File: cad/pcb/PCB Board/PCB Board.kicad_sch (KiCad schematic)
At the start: 40 parts, among them J1 USB4105, J2 S2B-PH-K-S, Q1 FDN340P, Q2 BSS138, SW1 PTS645, SW2 PTS645, SW3 PTS645, SW4 PTS645, SW5 PTS645, SW6 PTS645, SW7 SLW-1277545-3A-RA-N-D, U1 ESP32-C3-WROOM-02, U2 TLV75533PDYDR, U3 TP4057

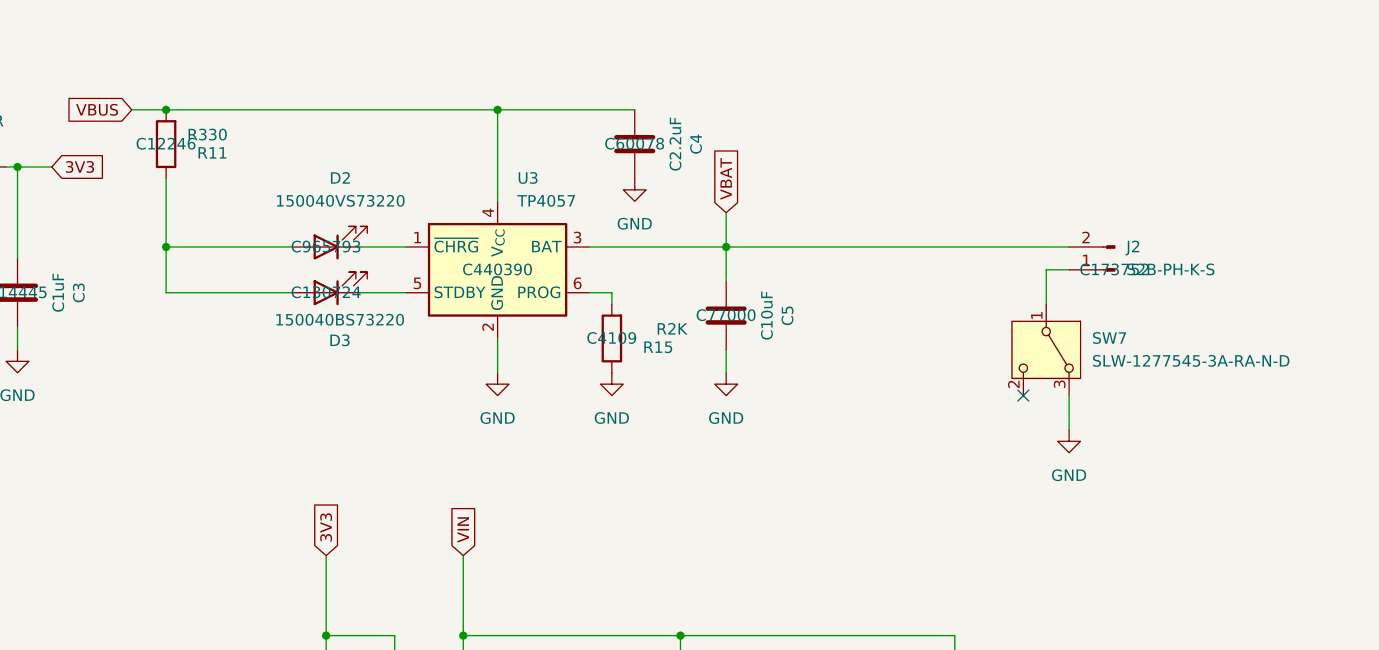
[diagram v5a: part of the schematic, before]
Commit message: updated with charging circuit
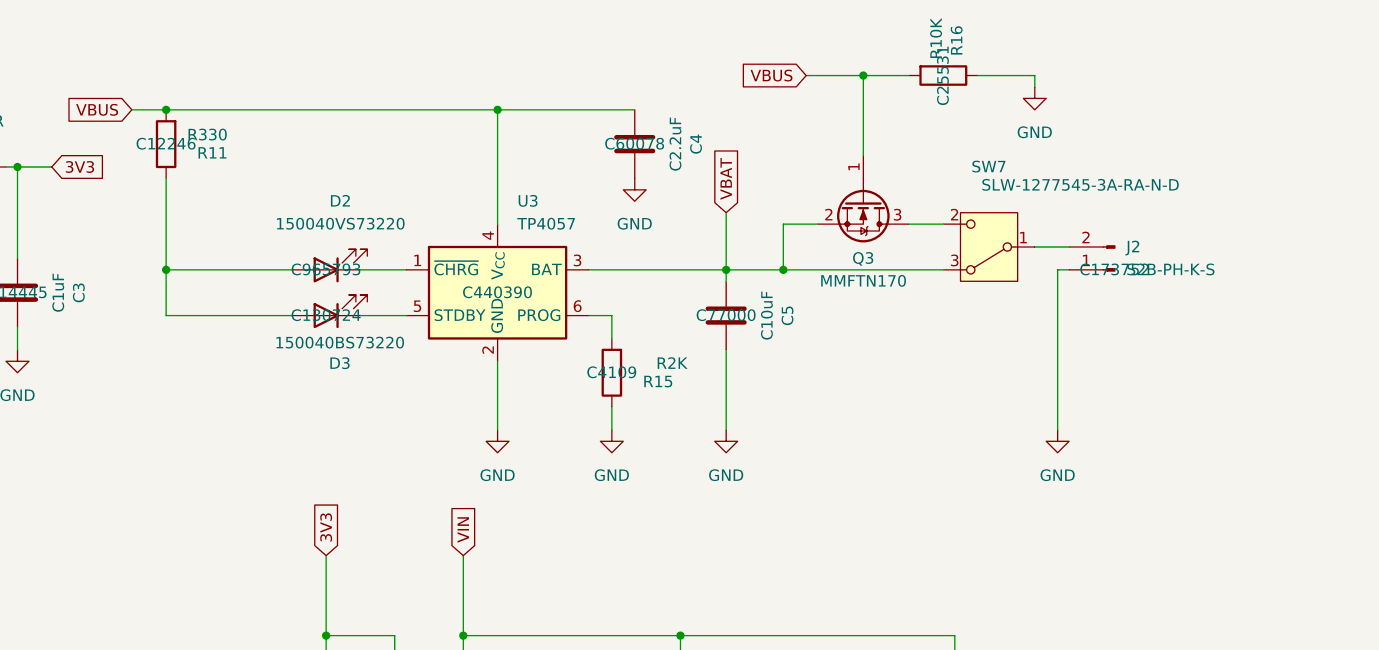
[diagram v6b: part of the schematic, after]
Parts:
- added Q3: MMFTN170, Package_TO_SOT_SMD:SOT-23, symbol Transistor_FET:BSS138
- added R16: R10K, Resistor_SMD:R_0402_1005Metric, symbol Device:R
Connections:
- net GND: now also J2.1 (Pin_1), R16.1; no longer SW7.3 (A)
- net VBAT: now also SW7.3 (A), Q3.2 (S); no longer J2.2 (Pin_2)
- net VBUS: now also Q3.1 (G), R16.2
- net at SW7.1 (B): now also J2.2 (Pin_2); no longer J2.1 (Pin_1)
- net at SW7.2 (C): now also Q3.3 (D)
- no-connect marks 9 -> 8
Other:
- moved on the sheet: D2, D3, R15, SW7, U3

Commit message: updated pcb design
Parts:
- Q3: value MMFTN170 -> NDS331N
- SW7: LCSC (none) -> C431547
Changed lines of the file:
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@@
 			)
 		)
-		(property "Datasheet" "https://www.we-https://www.mouser.de/datasheet/2/1628/slw_1277545_3a_ra_n_d-3510939.pdf"
+		(property "Datasheet" "https://www.lcsc.com/datasheet/lcsc_datasheet_1912111437_SHOU-HAN-SK12D07VG3_C431547.pdf"
 			(at 252.73 31.75 0)
 			(effects
@@
 		)
 		(property "Description" "Switch slide, single pole double throw"
+			(at 252.73 39.37 0)
+			(effects
+				(font
+					(size 1.27 1.27)
+				)
+				(hide yes)
+			)
+		)
+		(property "LCSC" "C431547"
 			(at 252.73 39.37 0)
 			(effects
@@
 			)
 		)
-		(property "Value" "MMFTN170"
+		(property "Value" "NDS331N"
 			(at 238.76 43.18 90)
 			(effects
@@
 			)
 		)
-		(property "Datasheet" "https://diotec.com/request/datasheet/mmftn170.pdf"
+		(property "Datasheet" "https://www.onsemi.com/download/data-sheet/pdf/nds331n-d.pdf"
 			(at 234.95 39.37 0)
 			(effects
@@
 			)
 		)
-		(property "Description" "50V Vds, 0.5A Id, N-Channel MOSFET, SOT-23"
+		(property "Description" "20V Vds, 0.5A Id, N-Channel MOSFET, SOT-23"
 			(at 238.76 34.29 0)
 			(effects

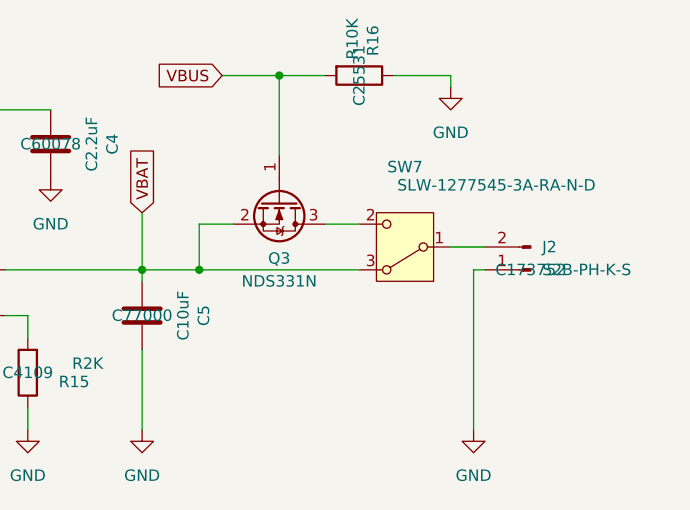
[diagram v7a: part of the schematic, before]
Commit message: fixed a wrong switch footprint
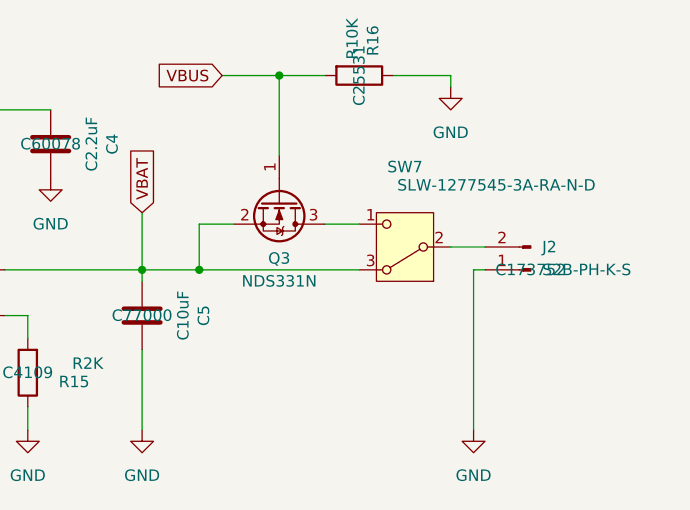
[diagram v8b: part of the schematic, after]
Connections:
- net at J2.2 (Pin_2): now also SW7.2 (B); no longer SW7.1 (B)
- net at Q3.3 (D): now also SW7.1 (C); no longer SW7.2 (C)
